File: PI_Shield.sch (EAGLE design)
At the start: 78 parts, among them J10 T2I, J11 T2I, J12 T2I, J13 DF13-4P-1.25DSA, J14 DF13-4P-1.25DSA, J15 DF13-4P-1.25DSA, J16 T2I5P, Q1 220mA/50V/3.5Ω, Q2 220mA/50V/3.5Ω, Q3 220mA/50V/3.5Ω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

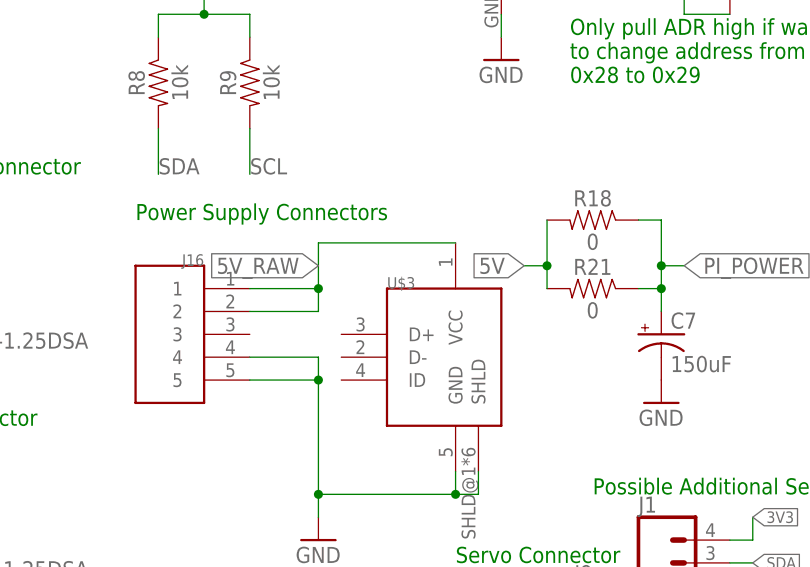
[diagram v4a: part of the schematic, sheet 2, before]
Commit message: naming USB connector and add notes for next year of which ICs to replace
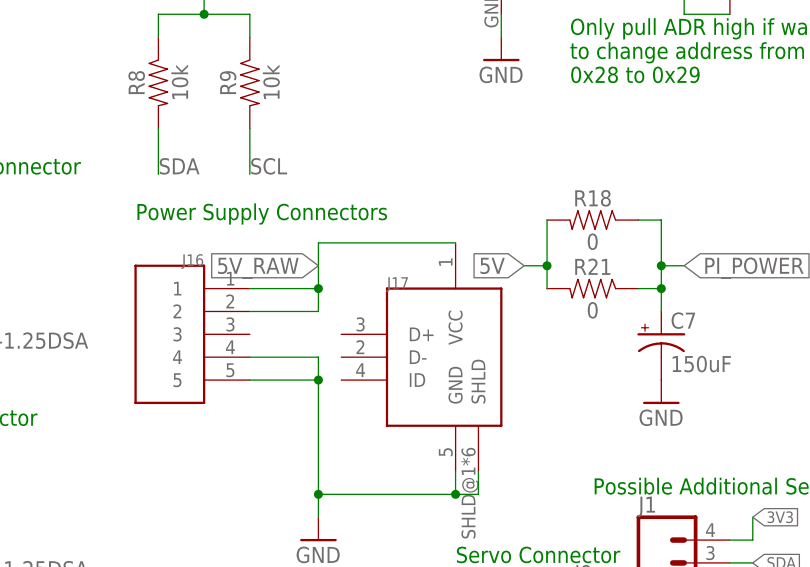
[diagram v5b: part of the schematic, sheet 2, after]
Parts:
- renumbered U$3 to J17
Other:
- note added: "Need to replace the sensor sensor with one in stock"
- note added: "Should replace the ADC with a cheaper one"
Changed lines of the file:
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@@
 <part name="U$5" library="Adafruit IMUs - BNO055 and FX" deviceset="ADAFRUIT-FXOS8700-FXAS21002" device=""/>
 <part name="GND31" library="supply1" library_urn="urn:adsk.eagle:library:371" deviceset="GND" device=""/>
-<part name="U$3" library="usb conn" deviceset="USB-MICRO" device=""/>
+<part name="J17" library="usb conn" deviceset="USB-MICRO" device=""/>
 <part name="U$7" library="MCR1101" deviceset="MCR1101" device=""/>
 <part name="R22" library="SparkFun-Resistors" library_urn="urn:adsk.eagle:library:532" deviceset="RESISTOR" device="0603" package3d_urn="urn:adsk.eagle:package:39650/1" value="0"/>
@@
 <attribute name="VALUE" x="149.86" y="121.92" size="1.778" layer="96"/>
 </instance>
-<instance part="U$3" gate="G$1" x="205.74" y="96.52" smashed="yes">
+<instance part="J17" gate="G$1" x="205.74" y="96.52" smashed="yes">
 <attribute name="NAME" x="203.2" y="99.06" size="1.27" layer="95"/>
 </instance>
@@
 <pinref part="J16" gate="&gt;NAME" pin="4"/>
 <pinref part="J16" gate="&gt;NAME" pin="5"/>
-<pinref part="U$3" gate="G$1" pin="SHLD"/>
+<pinref part="J17" gate="G$1" pin="SHLD"/>
 <wire x1="195.58" y1="76.2" x2="195.58" y2="73.66" width="0.1524" layer="91"/>
 <wire x1="213.36" y1="78.74" x2="213.36" y2="76.2" width="0.1524" layer="91"/>
 <wire x1="213.36" y1="76.2" x2="210.82" y2="76.2" width="0.1524" layer="91"/>
-<pinref part="U$3" gate="G$1" pin="GND"/>
+<pinref part="J17" gate="G$1" pin="GND"/>
 <wire x1="210.82" y1="76.2" x2="195.58" y2="76.2" width="0.1524" layer="91"/>
 <wire x1="210.82" y1="76.2" x2="210.82" y2="78.74" width="0.1524" layer="91"/>
@@
 <pinref part="J16" gate="&gt;NAME" pin="2"/>
 <label x="195.58" y="101.6" size="1.778" layer="95" rot="R180" xref="yes"/>
-<pinref part="U$3" gate="G$1" pin="VCC"/>
+<pinref part="J17" gate="G$1" pin="VCC"/>
 <wire x1="210.82" y1="104.14" x2="195.58" y2="104.14" width="0.1524" layer="91"/>
 <wire x1="195.58" y1="104.14" x2="195.58" y2="99.06" width="0.1524" layer="91"/>
@@
 <text x="81.28" y="63.5" size="1.778" layer="91">Circuit to Reset
 Overcurrent Fault</text>
+<text x="73.66" y="111.76" size="1.778" layer="91">Need to replace the sensor sensor with one in stock</text>
+<text x="129.54" y="162.56" size="1.778" layer="91">Should replace the ADC with a cheaper one</text>
 </plain>
 <instances>

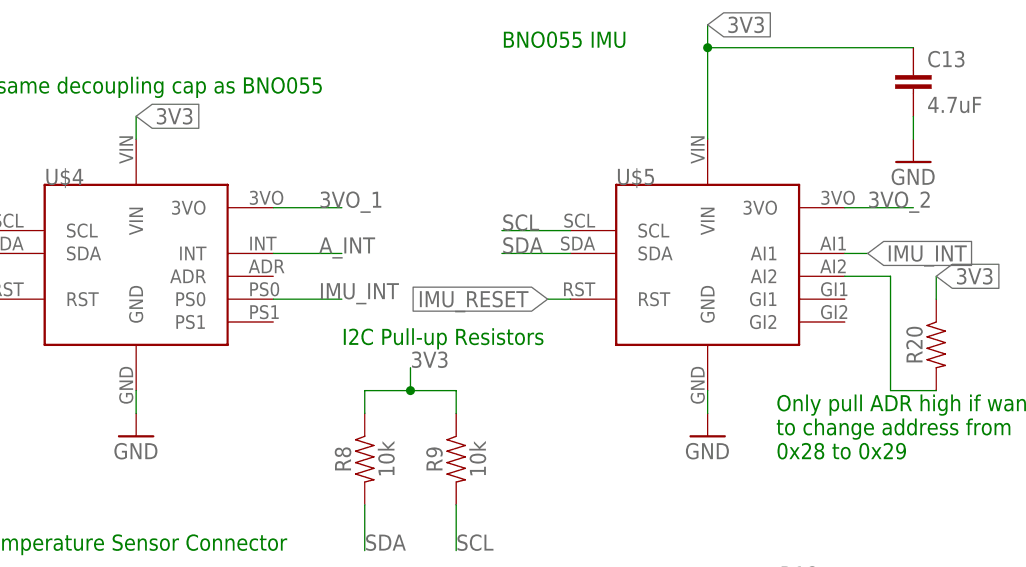
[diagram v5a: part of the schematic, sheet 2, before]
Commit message: Fixed Swapped IMUs on Schematic
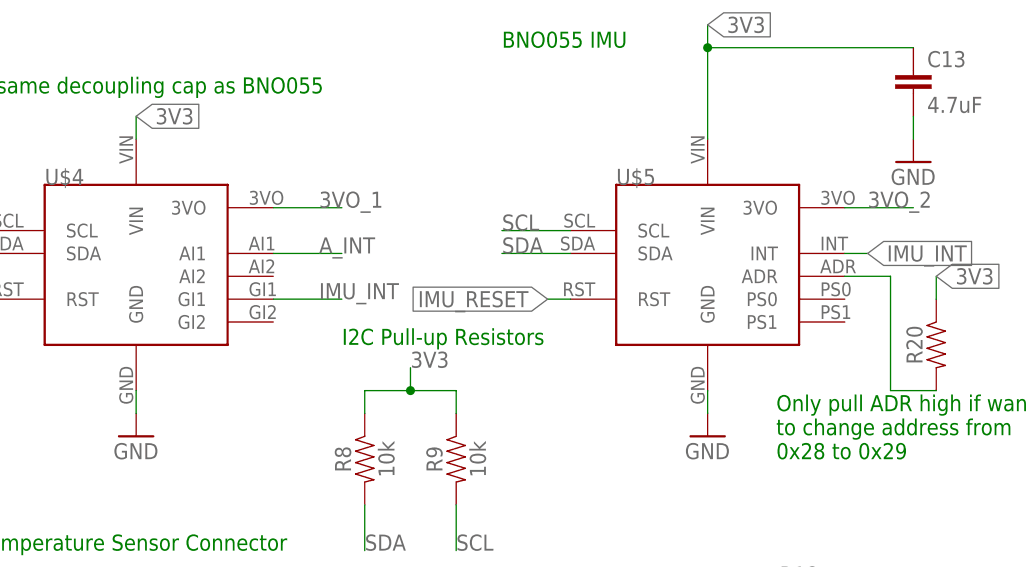
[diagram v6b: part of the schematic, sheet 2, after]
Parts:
- U$4: value ADAFRUIT-BNO055 -> ADAFRUIT-FXOS8700-FXAS21002; device Adafruit IMUs - BNO055 and FX:ADAFRUIT-BNO055 -> Adafruit IMUs - BNO055 and FX:ADAFRUIT-FXOS8700-FXAS21002
- U$5: value ADAFRUIT-FXOS8700-FXAS21002 -> ADAFRUIT-BNO055; device Adafruit IMUs - BNO055 and FX:ADAFRUIT-FXOS8700-FXAS21002 -> Adafruit IMUs - BNO055 and FX:ADAFRUIT-BNO055
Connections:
- net A_INT: now also U$4.AI1; no longer U$4.INT
- net IMU_INT: now also U$4.GI1, U$5.INT; no longer U$4.PS0, U$5.AI1
- net N$1: now also U$5.ADR; no longer U$5.AI2
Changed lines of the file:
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@@
 <?xml version="1.0" encoding="utf-8"?>
 <!DOCTYPE eagle SYSTEM "eagle.dtd">
-<eagle version="9.6.2">
+<eagle version="9.5.2">
 <drawing>
 <settings>
@@
 <part name="GND28" library="supply1" library_urn="urn:adsk.eagle:library:371" deviceset="GND" device=""/>
 <part name="R20" library="SparkFun-Resistors" library_urn="urn:adsk.eagle:library:532" deviceset="RESISTOR" device="0603" package3d_urn="urn:adsk.eagle:package:39650/1" value=""/>
-<part name="U$4" library="Adafruit IMUs - BNO055 and FX" deviceset="ADAFRUIT-BNO055" device=""/>
-<part name="U$5" library="Adafruit IMUs - BNO055 and FX" deviceset="ADAFRUIT-FXOS8700-FXAS21002" device=""/>
+<part name="U$4" library="Adafruit IMUs - BNO055 and FX" deviceset="ADAFRUIT-FXOS8700-FXAS21002" device=""/>
+<part name="U$5" library="Adafruit IMUs - BNO055 and FX" deviceset="ADAFRUIT-BNO055" device=""/>
 <part name="GND31" library="supply1" library_urn="urn:adsk.eagle:library:371" deviceset="GND" device=""/>
 <part name="J17" library="usb conn" deviceset="USB-MICRO" device=""/>
@@
 <label x="233.68" y="144.78" size="1.778" layer="95" xref="yes"/>
 <wire x1="231.14" y1="144.78" x2="233.68" y2="144.78" width="0.1524" layer="91"/>
-<pinref part="U$5" gate="G$1" pin="AI1"/>
+<pinref part="U$5" gate="G$1" pin="INT"/>
 </segment>
 <segment>
@@
 </segment>
 <segment>
-<pinref part="U$4" gate="G$1" pin="PS0"/>
+<pinref part="U$4" gate="G$1" pin="GI1"/>
 <wire x1="167.64" y1="139.7" x2="175.26" y2="139.7" width="0.1524" layer="91"/>
 <label x="172.72" y="139.7" size="1.778" layer="95"/>
@@
 <wire x1="236.22" y1="129.54" x2="241.3" y2="129.54" width="0.1524" layer="91"/>
 <pinref part="R20" gate="G$1" pin="2"/>
-<pinref part="U$5" gate="G$1" pin="AI2"/>
+<pinref part="U$5" gate="G$1" pin="ADR"/>
 </segment>
 </net>
@@
 <net name="A_INT" class="0">
 <segment>
-<pinref part="U$4" gate="G$1" pin="INT"/>
+<pinref part="U$4" gate="G$1" pin="AI1"/>
 <wire x1="167.64" y1="144.78" x2="175.26" y2="144.78" width="0.1524" layer="91"/>
 <label x="172.72" y="144.78" size="1.778" layer="95"/>

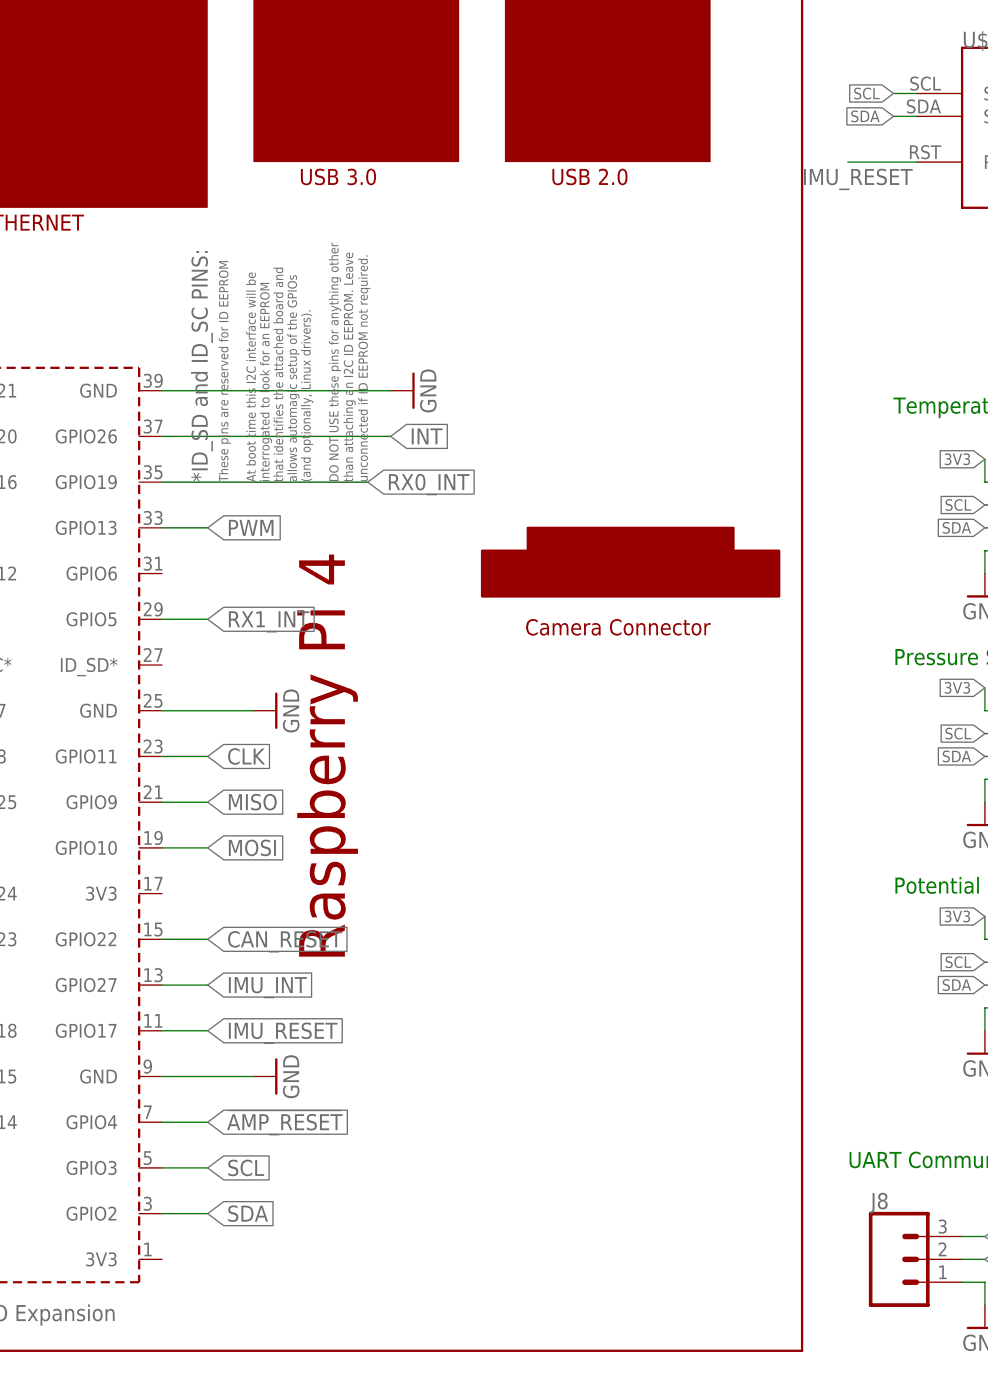
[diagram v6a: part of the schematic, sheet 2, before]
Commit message: Updated Parts from Updated X13 Parts Library
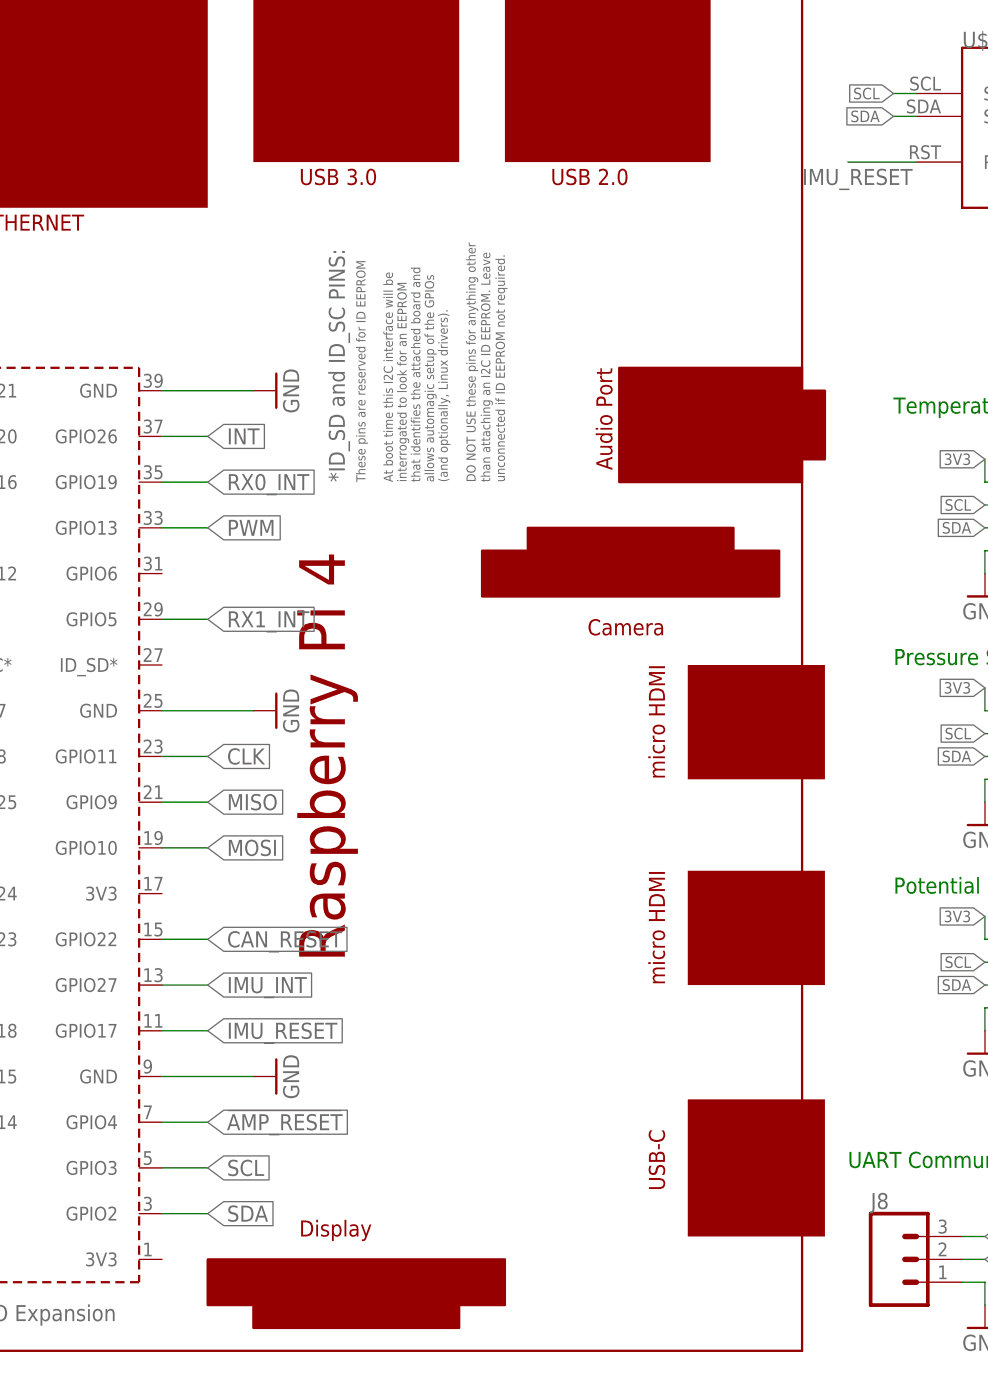
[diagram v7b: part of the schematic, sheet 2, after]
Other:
- moved on the sheet: U$7
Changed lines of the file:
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@@
 <attribute name="VALUE" x="5.08" y="101.6" size="1.778" layer="96" rot="R270"/>
 </instance>
-<instance part="GND45" gate="1" x="81.28" y="114.3" smashed="yes" rot="R90">
-<attribute name="VALUE" x="83.82" y="111.76" size="1.778" layer="96" rot="R90"/>
+<instance part="GND45" gate="1" x="66.04" y="114.3" smashed="yes" rot="R90">
+<attribute name="VALUE" x="68.58" y="111.76" size="1.778" layer="96" rot="R90"/>
 </instance>
 <instance part="GND46" gate="1" x="66.04" y="78.74" smashed="yes" rot="R90">
@@
 <segment>
 <pinref part="U$8" gate="G$1" pin="GND@39"/>
-<wire x1="53.34" y1="114.3" x2="78.74" y2="114.3" width="0.1524" layer="91"/>
+<wire x1="53.34" y1="114.3" x2="63.5" y2="114.3" width="0.1524" layer="91"/>
 <pinref part="GND45" gate="1" pin="GND"/>
 </segment>
@@
 <net name="INT" class="0">
 <segment>
-<label x="78.74" y="109.22" size="1.778" layer="95" xref="yes"/>
+<label x="58.42" y="109.22" size="1.778" layer="95" xref="yes"/>
 <pinref part="U$8" gate="G$1" pin="GPIO26"/>
-<wire x1="53.34" y1="109.22" x2="78.74" y2="109.22" width="0.1524" layer="91"/>
+<wire x1="53.34" y1="109.22" x2="58.42" y2="109.22" width="0.1524" layer="91"/>
 </segment>
 </net>
@@
 <net name="RX0_INT" class="0">
 <segment>
-<label x="76.2" y="104.14" size="1.778" layer="95" xref="yes"/>
+<label x="58.42" y="104.14" size="1.778" layer="95" xref="yes"/>
 <pinref part="U$8" gate="G$1" pin="GPIO19"/>
-<wire x1="53.34" y1="104.14" x2="76.2" y2="104.14" width="0.1524" layer="91"/>
-</segment>
-</net>
+<wire x1="53.34" y1="104.14" x2="58.42" y2="104.14" width="0.1524" layer="91"/>
+</segment>
+</net>
